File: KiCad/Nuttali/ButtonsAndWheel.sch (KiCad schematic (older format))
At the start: 20 parts, among them SW10 SW_Push, SW3 SW_Push, SW4 SW_Push, SW5 SW_Push, SW6 SW_Push, SW7 SW_Push, SW8 Rotary_Encoder

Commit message: Working on the new pcb
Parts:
- added J3, J4: Conn_01x03_Male, Connector_PinSocket_2.54mm:PinSocket_1x03_P2.54mm_Vertical, symbol Connector:Conn_01x03_Male
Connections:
- wire segments 44 -> 53
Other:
- note added: "To connect the side buttons since they will be on different pcb"
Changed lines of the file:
@@
-$EndComp
-$Comp
-L power:+3.3V #PWR0146
-U 1 1 602454F4
-P 1300 5150
-F 0 "#PWR0146" H 1300 5000 50  0001 C CNN
-F 1 "+3.3V" H 1315 5323 50  0000 C CNN
-F 2 "" H 1300 5150 50  0001 C CNN
-F 3 "" H 1300 5150 50  0001 C CNN
-	1    1300 5150
-	1    0    0    -1
 $EndComp
 $Comp
@@
 $EndComp
 Wire Wire Line
-	1300 5150 1400 5150
-Wire Wire Line
 	1800 5150 1850 5150
 Wire Wire Line
@@
 L power:+3.3V #PWR0147
 U 1 1 6027821D
-P 1300 5850
-F 0 "#PWR0147" H 1300 5700 50  0001 C CNN
-F 1 "+3.3V" H 1315 6023 50  0000 C CNN
-F 2 "" H 1300 5850 50  0001 C CNN
-F 3 "" H 1300 5850 50  0001 C CNN
-	1    1300 5850
+P 1250 6550
+F 0 "#PWR0147" H 1250 6400 50  0001 C CNN
+F 1 "+3.3V" H 1265 6723 50  0000 C CNN
+F 2 "" H 1250 6550 50  0001 C CNN
+F 3 "" H 1250 6550 50  0001 C CNN
+	1    1250 6550
 	1    0    0    -1
 $EndComp
@@
 L Device:R R10
 U 1 1 60278223
-P 2000 5850
-F 0 "R10" H 2070 5896 50  0000 L CNN
-F 1 "10k" H 2070 5805 50  0000 L CNN
-F 2 "Resistor_SMD:R_0805_2012Metric_Pad1.20x1.40mm_HandSolder" V 1930 5850 50  0001 C CNN
-F 3 "~" H 2000 5850 50  0001 C CNN
-	1    2000 5850
-	0    -1   -1   0
-$EndComp
-Wire Wire Line
-	1300 5850 1400 5850
-Wire Wire Line
-	1800 5850 1850 5850
-Text GLabel 2250 5150 2    50   Output ~ 0
+P 1950 5600
+F 0 "R10" H 2020 5646 50  0000 L CNN
+F 1 "10k" H 2020 5555 50  0000 L CNN
+F 2 "Resistor_SMD:R_0805_2012Metric_Pad1.20x1.40mm_HandSolder" V 1880 5600 50  0001 C CNN
+F 3 "~" H 1950 5600 50  0001 C CNN
+	1    1950 5600
+	0    -1   -1   0
+$EndComp
+Wire Wire Line
+	1750 5600 1800 5600
+Text GLabel 2050 6350 0    50   Output ~ 0
 SideFront
-Text GLabel 2250 5850 2    50   Output ~ 0
+Text GLabel 2050 6450 0    50   Output ~ 0
 SideBack
 $Comp
@@
 L Switch:SW_Push SW6
 U 1 1 6026F191
-P 1600 5850
-F 0 "SW6" H 1600 6135 50  0000 C CNN
-F 1 "SW_Push" H 1600 6044 50  0000 C CNN
-F 2 "Button_Switch_SMD:SW_Push_SPST_NO_Alps_SKRK" H 1600 6050 50  0001 C CNN
-F 3 "~" H 1600 6050 50  0001 C CNN
-	1    1600 5850
+P 1550 5600
+F 0 "SW6" H 1550 5885 50  0000 C CNN
+F 1 "SW_Push" H 1550 5794 50  0000 C CNN
+F 2 "Button_Switch_SMD:SW_Push_SPST_NO_Alps_SKRK" H 1550 5800 50  0001 C CNN
+F 3 "~" H 1550 5800 50  0001 C CNN
+	1    1550 5600
 	1    0    0    -1
 $EndComp
@@
 $EndComp
 Wire Wire Line
-	2150 5850 2250 5850
+	2100 5600 2200 5600
 Wire Notes Line
 	3100 550  3100 7700
+$Comp
+L Connector:Conn_01x03_Male J4
+U 1 1 6025B611
+P 2750 5300
+F 0 "J4" H 2858 5581 50  0000 C CNN
+F 1 "Conn_01x03_Male" H 2858 5490 50  0000 C CNN
+F 2 "Connector_PinSocket_2.54mm:PinSocket_1x03_P2.54mm_Vertical" H 2750 5300 50  0001 C CNN
+F 3 "~" H 2750 5300 50  0001 C CNN
+	1    2750 5300
+	-1   0    0    1
+$EndComp
+Wire Wire Line
+	2250 5200 2250 5150
+Wire Wire Line
+	2250 5200 2550 5200
+Wire Wire Line
+	2200 5600 2200 5300
+Wire Wire Line
+	2200 5300 2550 5300
+Wire Wire Line
+	2550 5400 2550 5850
+Wire Wire Line
+	2550 5850 950  5850
+Wire Wire Line
+	950  5850 950  5600
+Connection ~ 950  5600
+Wire Wire Line
+	950  5600 950  5150
+Wire Wire Line
+	950  5600 1350 5600
+Wire Wire Line
+	950  5150 1400 5150
+$Comp
+L Connector:Conn_01x03_Male J3
+U 1 1 6029AD59
+P 2250 6450
+F 0 "J3" H 2358 6731 50  0000 C CNN
+F 1 "Conn_01x03_Male" H 2358 6640 50  0000 C CNN
+F 2 "Connector_PinSocket_2.54mm:PinSocket_1x03_P2.54mm_Vertical" H 2250 6450 50  0001 C CNN
+F 3 "~" H 2250 6450 50  0001 C CNN
+	1    2250 6450
+	-1   0    0    1
+$EndComp
+Wire Wire Line
+	2050 6550 1250 6550
+Text Notes 500  6000 0    50   ~ 0
+To connect the side buttons since they will be on different pcb
 $EndSCHEMATC

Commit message: extended the pcb board with 2 mm to right
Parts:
- C27, C28, C29, C30: symbol Device:C -> Nuttali-rescue:C-Device
- D4: symbol Device:LED -> Nuttali-rescue:LED-Device
- J3, J4: symbol Connector:Conn_01x03_Male -> Nuttali-rescue:Conn_01x03_Male-Connector
- R10, R11, R12, R13, R15, R7, R8, R9: symbol Device:R -> Nuttali-rescue:R-Device
- SW10, SW3, SW4, SW5, SW6, SW7: symbol Switch:SW_Push -> Nuttali-rescue:SW_Push-Switch
- SW8: symbol Device:Rotary_Encoder -> Nuttali-rescue:Rotary_Encoder-Device
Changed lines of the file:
@@
 $EndDescr
 $Comp
-L power:+3.3V #PWR0140
+L Nuttali-rescue:+3.3V-power #PWR0140
 U 1 1 6023138D
 P 1800 800
@@
 $EndComp
 $Comp
-L Device:R R7
+L Nuttali-rescue:R-Device R7
 U 1 1 602321F1
 P 1800 1050
@@
 $EndComp
 $Comp
-L Device:C C27
+L Nuttali-rescue:C-Device C27
 U 1 1 60232EB4
 P 1800 1600
@@
 	1800 1350 2350 1350
 $Comp
-L power:GND #PWR0141
+L Nuttali-rescue:GND-power #PWR0141
 U 1 1 602361A1
 P 1150 1450
@@
 $EndComp
 $Comp
-L power:GND #PWR0142
+L Nuttali-rescue:GND-power #PWR0142
 U 1 1 602374C1
 P 1800 1850
@@
 $EndComp
 $Comp
-L power:+3.3V #PWR0143
+L Nuttali-rescue:+3.3V-power #PWR0143
 U 1 1 602440B2
 P 1800 2500
@@
 $EndComp
 $Comp
-L Device:R R8
+L Nuttali-rescue:R-Device R8
 U 1 1 602440B8
 P 1800 2750
@@
 $EndComp
 $Comp
-L Device:C C28
+L Nuttali-rescue:C-Device C28
 U 1 1 602440BE
 P 1800 3300
@@
 	1800 3050 2350 3050
 $Comp
-L power:GND #PWR0144
+L Nuttali-rescue:GND-power #PWR0144
 U 1 1 602440CC
 P 1150 3150
@@
 $EndComp
 $Comp
-L power:GND #PWR0145
+L Nuttali-rescue:GND-power #PWR0145
 U 1 1 602440D2
 P 1800 3550
@@
 $EndComp
 $Comp
-L Device:R R9
+L Nuttali-rescue:R-Device R9
 U 1 1 602454FA
 P 2000 5150
@@
 	2150 5150 2250 5150
 $Comp
-L power:+3.3V #PWR0147
+L Nuttali-rescue:+3.3V-power #PWR0147
 U 1 1 6027821D
 P 1250 6550
@@
 $EndComp
 $Comp
-L Device:R R10
+L Nuttali-rescue:R-Device R10
 U 1 1 60278223
 P 1950 5600
@@
 SideBack
 $Comp
-L power:+3.3V #PWR0148
+L Nuttali-rescue:+3.3V-power #PWR0148
 U 1 1 602BC22A
 P 4400 2450
@@
 $EndComp
 $Comp
-L Device:R R13
+L Nuttali-rescue:R-Device R13
 U 1 1 602BC230
 P 5100 2450
@@
 WheelButton
 $Comp
-L power:+3.3V #PWR0150
+L Nuttali-rescue:+3.3V-power #PWR0150
 U 1 1 602BED6F
 P 9150 3800
@@
 $EndComp
 $Comp
-L Device:R R15
+L Nuttali-rescue:R-Device R15
 U 1 1 602BED75
 P 9850 3800
@@
 Turbo
 $Comp
-L Device:LED D4
+L Nuttali-rescue:LED-Device D4
 U 1 1 602CBCDE
 P 9750 3350
@@
 $EndComp
 $Comp
-L power:GND #PWR0152
+L Nuttali-rescue:GND-power #PWR0152
 U 1 1 602CF144
 P 10250 3400
@@
 Top buttons
 $Comp
-L Device:Rotary_Encoder SW8
+L Nuttali-rescue:Rotary_Encoder-Device SW8
 U 1 1 60310A0D
 P 5200 3650
@@
 $EndComp
 $Comp
-L Device:C C29
+L Nuttali-rescue:C-Device C29
 U 1 1 60318A18
 P 4200 3450
@@
 $EndComp
 $Comp
-L Device:C C30
+L Nuttali-rescue:C-Device C30
 U 1 1 6031913E
 P 4200 3850
@@
 $EndComp
 $Comp
-L Device:R R11
+L Nuttali-rescue:R-Device R11
 U 1 1 6031998E
 P 4650 3200
@@
 $EndComp
 $Comp
-L Device:R R12
+L Nuttali-rescue:R-Device R12
 U 1 1 6031A38F
 P 4650 4200
@@
 	4650 3650 4900 3650
 $Comp
-L power:GND #PWR0153
+L Nuttali-rescue:GND-power #PWR0153
 U 1 1 6032A748
 P 4650 3700
@@
 WheelB
 $Comp
-L Switch:SW_Push SW3
+L Nuttali-rescue:SW_Push-Switch SW3
 U 1 1 6026C8AE
 P 1350 1350
@@
 $EndComp
 $Comp
-L Switch:SW_Push SW4
+L Nuttali-rescue:SW_Push-Switch SW4
 U 1 1 6026D38D
 P 1350 3050
@@
 $EndComp
 $Comp
-L Switch:SW_Push SW5
+L Nuttali-rescue:SW_Push-Switch SW5
 U 1 1 6026DDAA
 P 1600 5150
@@
 $EndComp
 $Comp
-L Switch:SW_Push SW6
+L Nuttali-rescue:SW_Push-Switch SW6
 U 1 1 6026F191
 P 1550 5600
@@
 $EndComp
 $Comp
-L Switch:SW_Push SW7
+L Nuttali-rescue:SW_Push-Switch SW7
 U 1 1 6026F8D9
 P 4700 2450
@@
 $EndComp
 $Comp
-L Switch:SW_Push SW10
+L Nuttali-rescue:SW_Push-Switch SW10
 U 1 1 602726D9
 P 9450 3800
@@
 	3100 550  3100 7700
 $Comp
-L Connector:Conn_01x03_Male J4
+L Nuttali-rescue:Conn_01x03_Male-Connector J4
 U 1 1 6025B611
 P 2750 5300
+AR Path="/6025B611" Ref="J4"  Part="1"
+AR Path="/6022DC9B/6025B611" Ref="J4"  Part="1"
 F 0 "J4" H 2858 5581 50  0000 C CNN
 F 1 "Conn_01x03_Male" H 2858 5490 50  0000 C CNN
@@
 	950  5150 1400 5150
 $Comp
-L Connector:Conn_01x03_Male J3
+L Nuttali-rescue:Conn_01x03_Male-Connector J3
 U 1 1 6029AD59
 P 2250 6450
+AR Path="/6029AD59" Ref="J3"  Part="1"
+AR Path="/6022DC9B/6029AD59" Ref="J3"  Part="1"
 F 0 "J3" H 2358 6731 50  0000 C CNN
 F 1 "Conn_01x03_Male" H 2358 6640 50  0000 C CNN

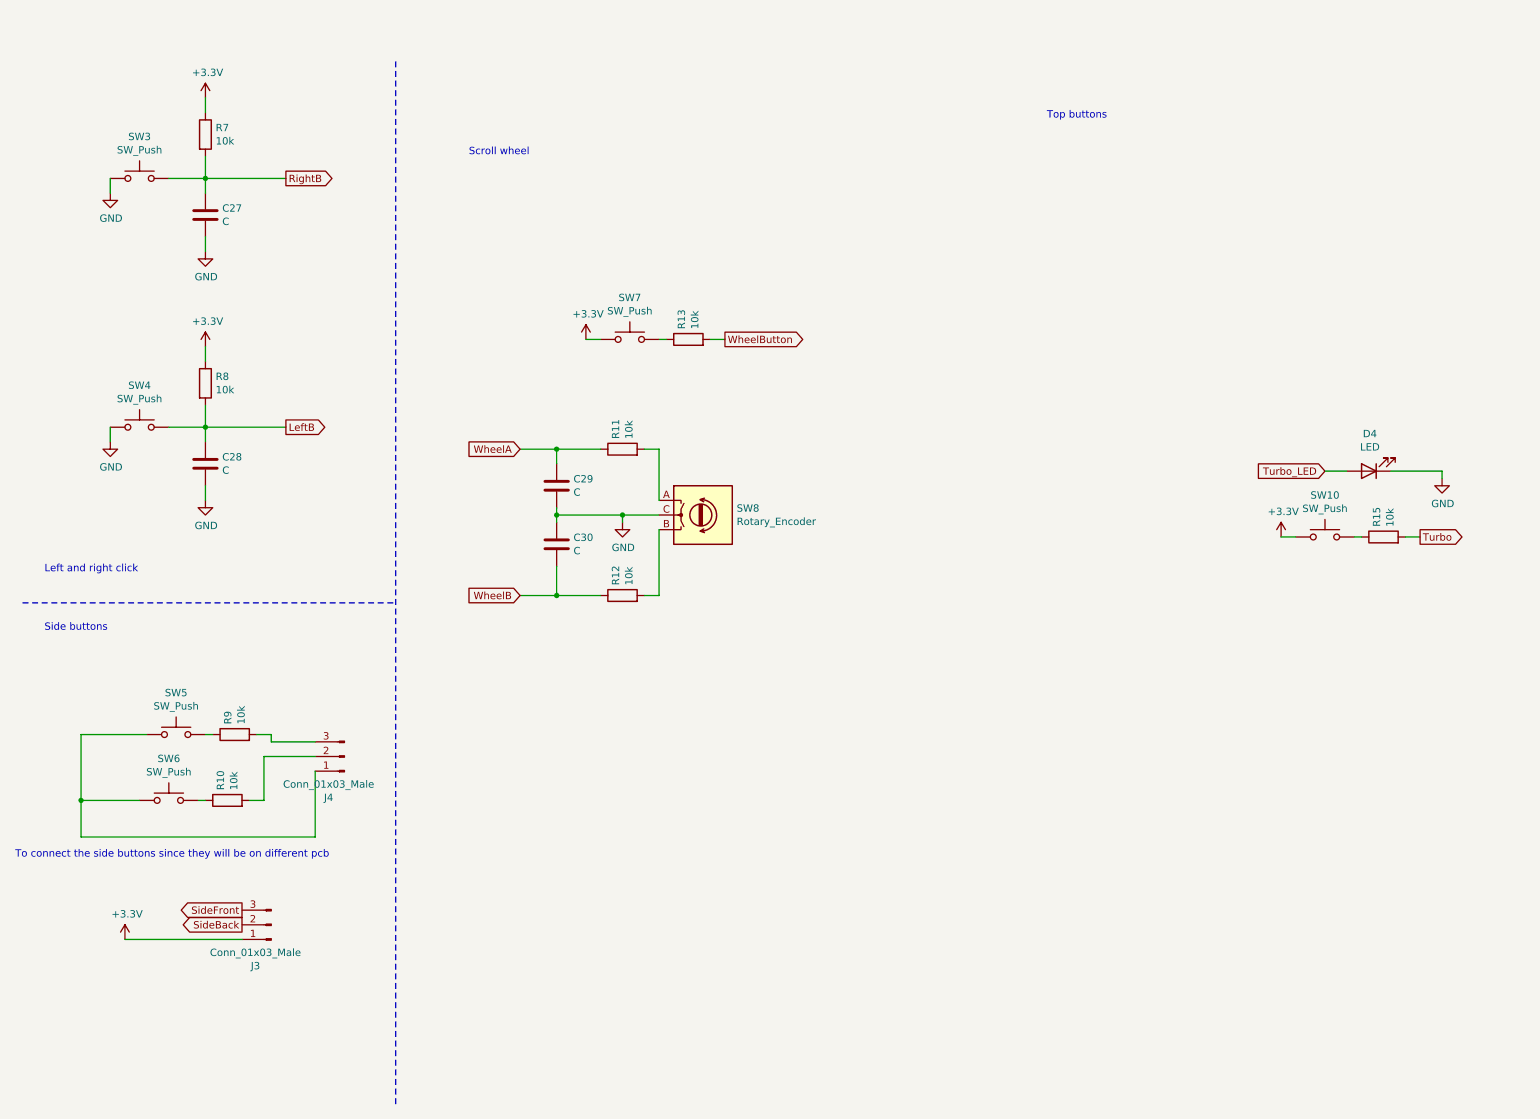
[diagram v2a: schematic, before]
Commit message: Fixed almost all footprints and nearly the layout of the pcb
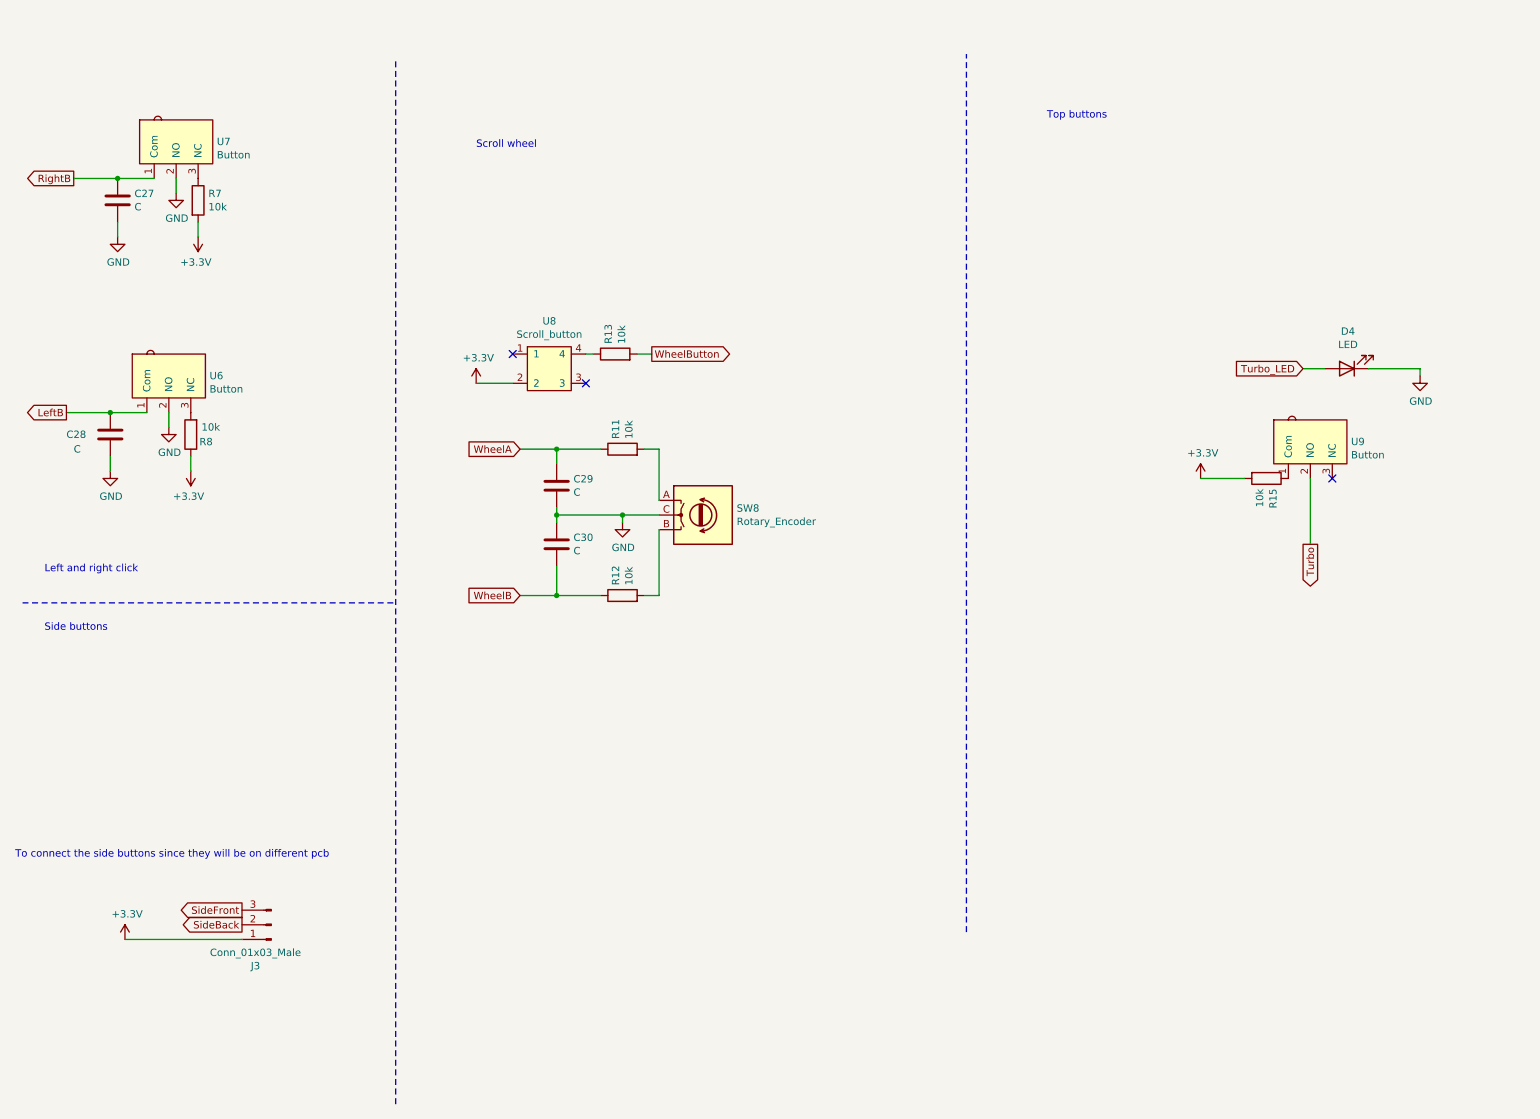
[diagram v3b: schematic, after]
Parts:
- removed J4: Conn_01x03_Male, Connector_PinSocket_2.54mm:PinSocket_1x03_P2.54mm_Vertical, symbol Nuttali-rescue:Conn_01x03_Male-Connector
- removed R10, R9: 10k, Resistor_SMD:R_0805_2012Metric_Pad1.20x1.40mm_HandSolder, symbol Nuttali-rescue:R-Device
- removed SW10, SW3, SW4, SW5, SW6, SW7: SW_Push, Button_Switch_SMD:SW_Push_SPST_NO_Alps_SKRK, symbol Nuttali-rescue:SW_Push-Switch
- added U6, U7, U9: Button, Nuttali:D2F-5, symbol new_components:Button
- added U8: Scroll_button, Nuttali:Scroll_button, symbol new_components:Scroll_button
- D4: footprint LED_SMD:LED_0201_0603Metric_Pad0.64x0.40mm_HandSolder -> Nuttali:LED
- SW8: footprint Rotary_Encoder:RotaryEncoder_Alps_EC11E_Vertical_H20mm_CircularMountingHoles -> Nuttali:Encoder
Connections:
- net +3V3: now also R15.2, R7.2, U8.2; no longer R7.1
- net GND: now also U6.2 (NO), U7.2 (NO)
- net LeftB: now also U6.1 (Com); no longer R8.2
- net RightB: now also U7.1 (Com); no longer R7.2
- net Turbo: now also U9.2 (NO); no longer R15.2
- net at R13.1: now also U8.4
- net at R15.1: now also U9.1 (Com)
- new net: R7.1, U7.3 (NC)
- new net: R8.2, U6.3 (NC)
- no-connect marks 0 -> 3
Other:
- moved on the sheet: C27, C28, D4, R13, R15, R7, R8

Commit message: Finnished the pcb
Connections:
- net +3V3: now also R11.1, R12.2, R13.1; no longer U8.2
- net WheelA: now also R11.2, SW8.A; no longer R11.1
- net WheelB: now also SW8.B
- net WheelButton: now also U8.2; no longer R13.2
- net at U8.4: now also R13.2; no longer R13.1
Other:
- moved on the sheet: R11, R12, R13
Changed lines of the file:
@@
 L Nuttali-rescue:+3.3V-power #PWR0148
 U 1 1 602BC22A
-P 3650 2750
-F 0 "#PWR0148" H 3650 2600 50  0001 C CNN
-F 1 "+3.3V" H 3665 2923 50  0000 C CNN
-F 2 "" H 3650 2750 50  0001 C CNN
-F 3 "" H 3650 2750 50  0001 C CNN
-	1    3650 2750
+P 5000 2550
+F 0 "#PWR0148" H 5000 2400 50  0001 C CNN
+F 1 "+3.3V" H 5015 2723 50  0000 C CNN
+F 2 "" H 5000 2550 50  0001 C CNN
+F 3 "" H 5000 2550 50  0001 C CNN
+	1    5000 2550
 	1    0    0    -1
 $EndComp
@@
 L Nuttali-rescue:R-Device R13
 U 1 1 602BC230
-P 4600 2550
-F 0 "R13" H 4670 2596 50  0000 L CNN
-F 1 "10k" H 4670 2505 50  0000 L CNN
-F 2 "Resistor_SMD:R_0805_2012Metric_Pad1.20x1.40mm_HandSolder" V 4530 2550 50  0001 C CNN
-F 3 "~" H 4600 2550 50  0001 C CNN
-	1    4600 2550
-	0    -1   -1   0
-$EndComp
-Wire Wire Line
-	3650 2750 3900 2750
-Wire Wire Line
-	4400 2550 4450 2550
-Wire Wire Line
-	4750 2550 4850 2550
-Text GLabel 4850 2550 2    50   Output ~ 0
+P 4800 2550
+F 0 "R13" H 4870 2596 50  0000 L CNN
+F 1 "10k" H 4870 2505 50  0000 L CNN
+F 2 "Resistor_SMD:R_0805_2012Metric_Pad1.20x1.40mm_HandSolder" V 4730 2550 50  0001 C CNN
+F 3 "~" H 4800 2550 50  0001 C CNN
+	1    4800 2550
+	0    1    1    0
+$EndComp
+Wire Wire Line
+	4400 2550 4650 2550
+Wire Wire Line
+	5000 2550 4950 2550
+Wire Wire Line
+	3900 2750 3800 2750
+Text GLabel 3800 2750 0    50   Output ~ 0
 WheelButton
 $Comp
@@
 L Nuttali-rescue:R-Device R11
 U 1 1 6031998E
-P 4650 3200
-F 0 "R11" H 4720 3246 50  0000 L CNN
-F 1 "10k" H 4720 3155 50  0000 L CNN
-F 2 "Resistor_SMD:R_0805_2012Metric_Pad1.20x1.40mm_HandSolder" V 4580 3200 50  0001 C CNN
-F 3 "~" H 4650 3200 50  0001 C CNN
-	1    4650 3200
-	0    -1   -1   0
+P 5050 3200
+F 0 "R11" H 5120 3246 50  0000 L CNN
+F 1 "10k" H 5120 3155 50  0000 L CNN
+F 2 "Resistor_SMD:R_0805_2012Metric_Pad1.20x1.40mm_HandSolder" V 4980 3200 50  0001 C CNN
+F 3 "~" H 5050 3200 50  0001 C CNN
+	1    5050 3200
+	0    1    1    0
 $EndComp
 $Comp
 L Nuttali-rescue:R-Device R12
 U 1 1 6031A38F
-P 4650 4200
-F 0 "R12" H 4720 4246 50  0000 L CNN
-F 1 "10k" H 4720 4155 50  0000 L CNN
-F 2 "Resistor_SMD:R_0805_2012Metric_Pad1.20x1.40mm_HandSolder" V 4580 4200 50  0001 C CNN
-F 3 "~" H 4650 4200 50  0001 C CNN
-	1    4650 4200
+P 5050 4200
+F 0 "R12" H 5120 4246 50  0000 L CNN
+F 1 "10k" H 5120 4155 50  0000 L CNN
+F 2 "Resistor_SMD:R_0805_2012Metric_Pad1.20x1.40mm_HandSolder" V 4980 4200 50  0001 C CNN
+F 3 "~" H 5050 4200 50  0001 C CNN
+	1    5050 4200
 	0    -1   -1   0
 $EndComp
 Wire Wire Line
 	4900 3550 4900 3200
-Wire Wire Line
-	4900 3200 4800 3200
-Wire Wire Line
-	4500 3200 4200 3200
 Wire Wire Line
 	4200 3200 4200 3300
@@
 Wire Wire Line
 	4900 3750 4900 4200
-Wire Wire Line
-	4900 4200 4800 4200
-Wire Wire Line
-	4500 4200 4200 4200
 Wire Wire Line
 	4200 4200 4200 4000
@@
 Wire Wire Line
 	9350 3400 9350 3850
+Connection ~ 4900 3200
+Wire Wire Line
+	4200 3200 4900 3200
+$Comp
+L Nuttali-rescue:+3.3V-power #PWR0146
+U 1 1 604D0219
+P 5250 3200
+F 0 "#PWR0146" H 5250 3050 50  0001 C CNN
+F 1 "+3.3V" H 5265 3373 50  0000 C CNN
+F 2 "" H 5250 3200 50  0001 C CNN
+F 3 "" H 5250 3200 50  0001 C CNN
+	1    5250 3200
+	0    1    1    0
+$EndComp
+Wire Wire Line
+	5250 3200 5200 3200
+Connection ~ 4900 4200
+Wire Wire Line
+	4200 4200 4900 4200
+$Comp
+L Nuttali-rescue:+3.3V-power #PWR0149
+U 1 1 604D56F4
+P 5250 4200
+F 0 "#PWR0149" H 5250 4050 50  0001 C CNN
+F 1 "+3.3V" H 5265 4373 50  0000 C CNN
+F 2 "" H 5250 4200 50  0001 C CNN
+F 3 "" H 5250 4200 50  0001 C CNN
+	1    5250 4200
+	0    1    1    0
+$EndComp
+Wire Wire Line
+	5250 4200 5200 4200
 $EndSCHEMATC
